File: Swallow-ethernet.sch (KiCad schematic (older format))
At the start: 35 parts, among them P1 XTAG2, P10 CONN_14, P11 CONN_8, P12 CONN_3, P13 GPIO_2, P14 GPIO_1, P2 XMP16_TR_Link, P3 TR_Link_Out, P4 Mode_Select, U1 25MHz_ASE_CLK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

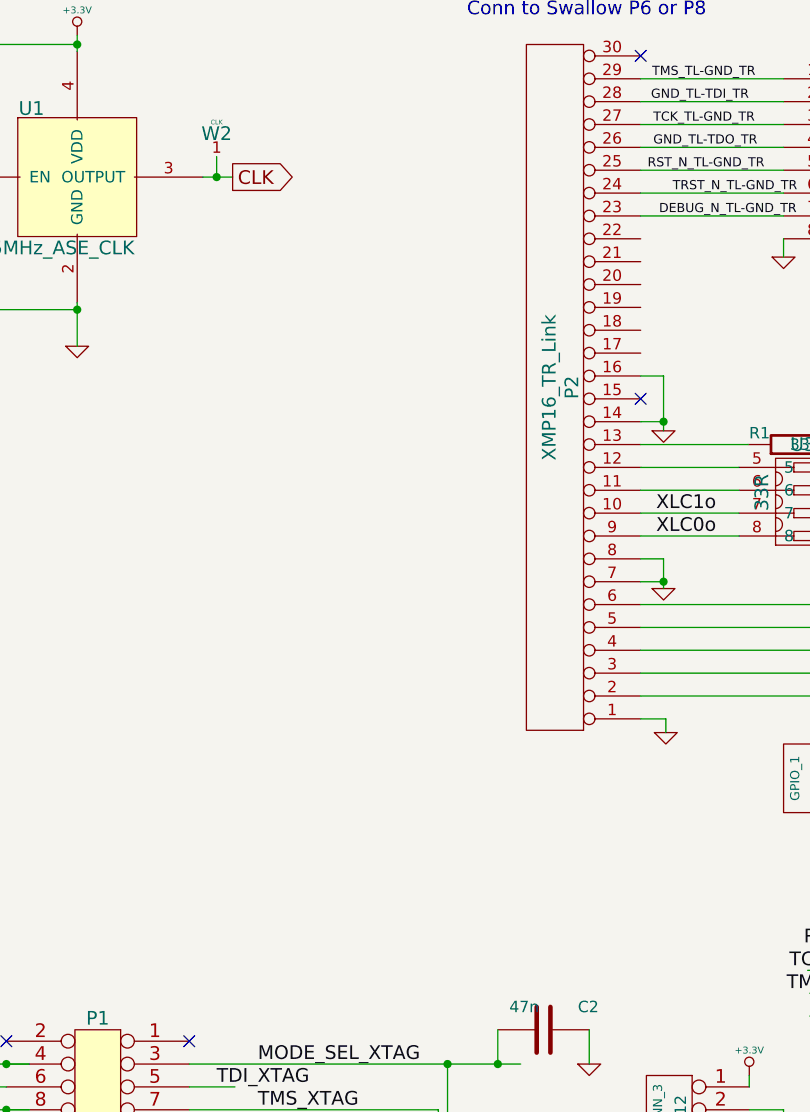
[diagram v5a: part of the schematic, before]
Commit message: Added clock buffer for L1 + ethernet MAC. Updated BOM.
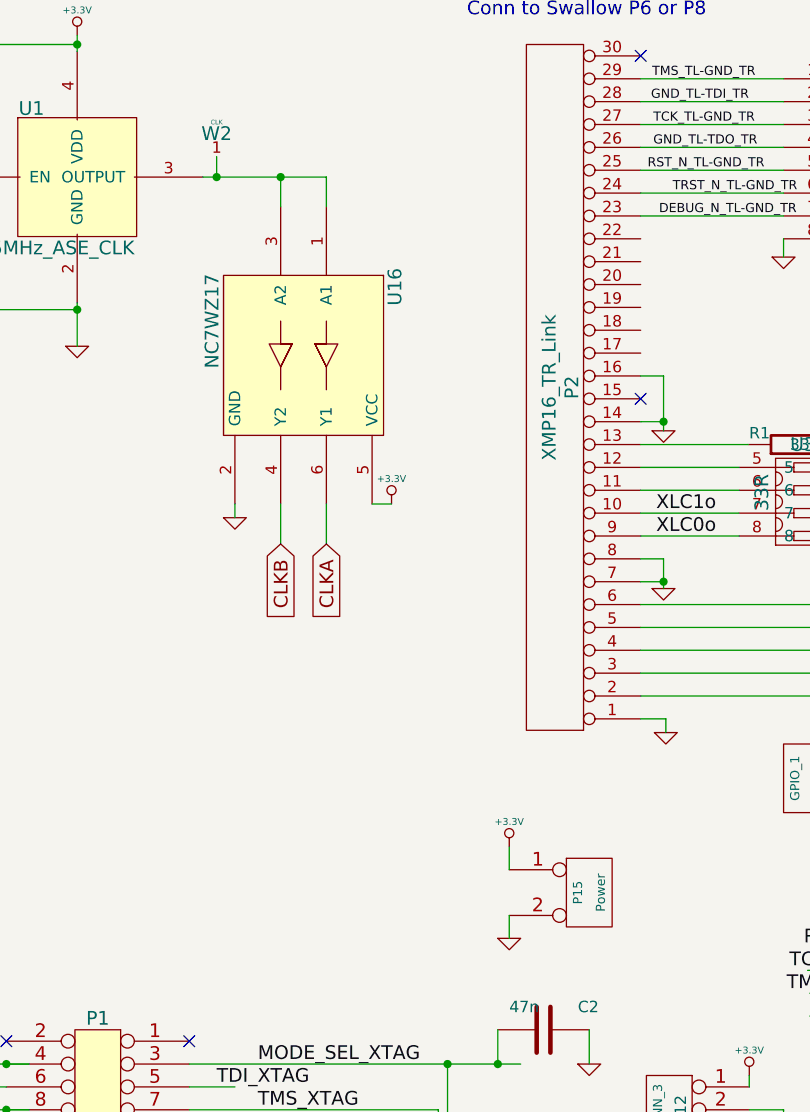
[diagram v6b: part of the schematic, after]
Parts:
- added P15: Power, symbol CONN_2
- added U16: NC7WZ17, symbol NC7WZ17
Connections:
- net labels added: CLKA, CLKB
- net labels removed: CLK
- wire segments 213 -> 221
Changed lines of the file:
@@
-EESchema Schematic File Version 2  date Thu 11 Oct 2012 12:37:16 BST
+EESchema Schematic File Version 2  date Thu 11 Oct 2012 17:02:03 BST
 LIBS:power
 LIBS:device
@@
 Comment4 ""
 $EndDescr
+Text GLabel 2750 2925 3    60   Input ~ 0
+CLKA
+Text GLabel 2550 2925 3    60   Input ~ 0
+CLKB
+Wire Wire Line
+	2750 2750 2750 2925
+Wire Wire Line
+	3035 2750 2950 2750
+Connection ~ 2550 1320
+Wire Wire Line
+	2210 1320 2750 1320
+Wire Wire Line
+	2750 1320 2750 1450
+Wire Wire Line
+	3550 4550 3550 4650
 Connection ~ 1250 740
 Connection ~ 1110 1260
@@
 Wire Wire Line
 	5115 2690 5285 2690
-Wire Wire Line
-	2210 1320 2340 1320
 Wire Wire Line
 	840  1030 840  740
@@
 Wire Notes Line
 	3450 7150 1450 7150
+Wire Wire Line
+	3550 4250 3550 4350
+Wire Wire Line
+	2550 1320 2550 1450
+Wire Wire Line
+	2350 2810 2350 2750
+Wire Wire Line
+	2550 2750 2550 2925
+$Comp
+L +3.3V #PWR5
+U 1 1 5076ECC9
+P 3035 2750
+F 0 "#PWR5" H 3035 2710 30  0001 C CNN
+F 1 "+3.3V" H 3035 2860 30  0000 C CNN
+	1    3035 2750
+	1    0    0    -1
+$EndComp
+$Comp
+L GND #PWR4
+U 1 1 5076ECC1
+P 2350 2810
+F 0 "#PWR4" H 2350 2810 30  0001 C CNN
+F 1 "GND" H 2350 2740 30  0001 C CNN
+	1    2350 2810
+	1    0    0    -1
+$EndComp
+$Comp
+L NC7WZ17 U16
+U 1 1 5076EC96
+P 2650 2100
+F 0 "U16" H 2350 2500 60  0000 C CNN
+F 1 "NC7WZ17" H 2500 1700 60  0000 C CNN
+	1    2650 2100
+	0    1    1    0
+$EndComp
+$Comp
+L +3.3V #PWR6
+U 1 1 5076E8F8
+P 3550 4250
+F 0 "#PWR6" H 3550 4210 30  0001 C CNN
+F 1 "+3.3V" H 3550 4360 30  0000 C CNN
+	1    3550 4250
+	1    0    0    -1
+$EndComp
+$Comp
+L GND #PWR7
+U 1 1 5076E8F3
+P 3550 4650
+F 0 "#PWR7" H 3550 4650 30  0001 C CNN
+F 1 "GND" H 3550 4580 30  0001 C CNN
+	1    3550 4650
+	1    0    0    -1
+$EndComp
+$Comp
+L CONN_2 P15
+U 1 1 5076E8EA
+P 3900 4450
+F 0 "P15" V 3850 4450 40  0000 C CNN
+F 1 "Power" V 3950 4450 40  0000 C CNN
+	1    3900 4450
+	1    0    0    -1
+$EndComp
 Text Notes 1750 7250 0    60   ~ 0
 Mechanicals
@@
 TMS_TL-GND_TR
 $Comp
-L +3.3V #PWR01
+L +3.3V #PWR13
 U 1 1 506DF2C0
 P 4600 5250
-F 0 "#PWR01" H 4600 5210 30  0001 C CNN
+F 0 "#PWR13" H 4600 5210 30  0001 C CNN
 F 1 "+3.3V" H 4600 5360 30  0000 C CNN
 	1    4600 5250
@@
 $EndComp
 $Comp
-L GND #PWR02
+L GND #PWR14
 U 1 1 506DF2B1
 P 4600 5550
-F 0 "#PWR02" H 4600 5550 30  0001 C CNN
+F 0 "#PWR14" H 4600 5550 30  0001 C CNN
 F 1 "GND" H 4600 5480 30  0001 C CNN
 	1    4600 5550
@@
 $EndComp
 $Comp
-L GND #PWR03
+L GND #PWR18
 U 1 1 506DF27B
 P 5850 5700
-F 0 "#PWR03" H 5850 5700 30  0001 C CNN
+F 0 "#PWR18" H 5850 5700 30  0001 C CNN
 F 1 "GND" H 5850 5630 30  0001 C CNN
 	1    5850 5700
@@
 $EndComp
 $Comp
-L +3.3V #PWR04
+L +3.3V #PWR17
 U 1 1 506DF26E
 P 5750 5550
-F 0 "#PWR04" H 5750 5510 30  0001 C CNN
+F 0 "#PWR17" H 5750 5510 30  0001 C CNN
 F 1 "+3.3V" H 5750 5660 30  0000 C CNN
 	1    5750 5550
@@
 $EndComp
 $Comp
-L GND #PWR05
+L GND #PWR16
 U 1 1 506DF266
 P 4750 6350
-F 0 "#PWR05" H 4750 6350 30  0001 C CNN
+F 0 "#PWR16" H 4750 6350 30  0001 C CNN
 F 1 "GND" H 4750 6280 30  0001 C CNN
 	1    4750 6350
@@
 $EndComp
 $Comp
-L GND #PWR06
+L GND #PWR15
 U 1 1 506D64CB
 P 4750 1670
-F 0 "#PWR06" H 4750 1670 30  0001 C CNN
+F 0 "#PWR15" H 4750 1670 30  0001 C CNN
 F 1 "GND" H 4750 1600 30  0001 C CNN
 	1    4750 1670
@@
 NoConn ~ 9815 910
 $Comp
-L GND #PWR07
+L GND #PWR24
 U 1 1 4F5BDE19
 P 9745 2550
-F 0 "#PWR07" H 9745 2550 30  0001 C CNN
+F 0 "#PWR24" H 9745 2550 30  0001 C CNN
 F 1 "GND" H 9745 2480 30  0001 C CNN
 	1    9745 2550
@@
 $EndComp
 $Comp
-L GND #PWR08
+L GND #PWR25
 U 1 1 506C85F4
 P 9815 3905
-F 0 "#PWR08" H 9815 3905 30  0001 C CNN
+F 0 "#PWR25" H 9815 3905 30  0001 C CNN
 F 1 "GND" H 9815 3835 30  0001 C CNN
 	1    9815 3905
@@
 $EndComp
 $Comp
-L +3.3V #PWR09
+L +3.3V #PWR19
 U 1 1 506A064F
 P 7185 4600
-F 0 "#PWR09" H 7185 4560 30  0001 C CNN
+F 0 "#PWR19" H 7185 4560 30  0001 C CNN
 F 1 "+3.3V" H 7185 4710 30  0000 C CNN
 	1    7185 4600
@@
 RESET_N
 $Comp
-L +3.3V #PWR010
+L +3.3V #PWR21
 U 1 1 506A0632
 P 8410 4970
-F 0 "#PWR010" H 8410 4930 30  0001 C CNN
+F 0 "#PWR21" H 8410 4930 30  0001 C CNN
 F 1 "+3.3V" H 8410 5080 30  0000 C CNN
 	1    8410 4970
@@
 $EndComp
 $Comp
-L GND #PWR011
+L GND #PWR20
 U 1 1 4F5BDEF3
 P 8355 4740
-F 0 "#PWR011" H 8355 4740 30  0001 C CNN
+F 0 "#PWR20" H 8355 4740 30  0001 C CNN
 F 1 "GND" H 8355 4670 30  0001 C CNN
 	1    8355 4740
@@
 $EndComp
 $Comp
-L GND #PWR012
+L GND #PWR23
 U 1 1 4F5BDE2C
 P 9715 3240
-F 0 "#PWR012" H 9715 3240 30  0001 C CNN
+F 0 "#PWR23" H 9715 3240 30  0001 C CNN
 F 1 "GND" H 9715 3170 30  0001 C CNN
 	1    9715 3240
@@
 $EndComp
 $Comp
-L GND #PWR013
+L GND #PWR30
 U 1 1 4F5BD965
 P 10490 5260
-F 0 "#PWR013" H 10490 5260 30  0001 C CNN
+F 0 "#PWR30" H 10490 5260 30  0001 C CNN
 F 1 "GND" H 10490 5190 30  0001 C CNN
 	1    10490 5260
@@
 $EndComp
 $Comp
-L GND #PWR014
+L GND #PWR27
 U 1 1 4F5BD8A9
 P 10050 6020
-F 0 "#PWR014" H 10050 6020 30  0001 C CNN
+F 0 "#PWR27" H 10050 6020 30  0001 C CNN
 F 1 "GND" H 10050 5950 30  0001 C CNN
 	1    10050 6020
@@
 $EndComp
 $Comp
-L GND #PWR015
+L GND #PWR29
 U 1 1 4F5BD89D
 P 10050 6980
-F 0 "#PWR015" H 10050 6980 30  0001 C CNN
+F 0 "#PWR29" H 10050 6980 30  0001 C CNN
 F 1 "GND" H 10050 6910 30  0001 C CNN
 	1    10050 6980
@@
 $EndComp
 $Comp
-L +3.3V #PWR016
+L +3.3V #PWR26
 U 1 1 4F5BD888
 P 10050 5260
-F 0 "#PWR016" H 10050 5220 30  0001 C CNN
+F 0 "#PWR26" H 10050 5220 30  0001 C CNN
 F 1 "+3.3V" H 10050 5370 30  0000 C CNN
 	1    10050 5260
@@
 RST_N_TL-GND_TR
 $Comp
-L GND #PWR017
+L GND #PWR12
 U 1 1 4F5BA318
 P 4235 3750
-F 0 "#PWR017" H 4235 3750 30  0001 C CNN
+F 0 "#PWR12" H 4235 3750 30  0001 C CNN
 F 1 "GND" H 4235 3680 30  0001 C CNN
 	1    4235 3750
@@
 $EndComp
 $Comp
-L GND #PWR018
+L GND #PWR10
 U 1 1 4F5BA2F7
 P 4225 2430
-F 0 "#PWR018" H 4225 2430 30  0001 C CNN
+F 0 "#PWR10" H 4225 2430 30  0001 C CNN
 F 1 "GND" H 4225 2360 30  0001 C CNN
 	1    4225 2430
@@
 $EndComp
 $Comp
-L GND #PWR019
+L GND #PWR11
 U 1 1 4F5BA2E3
 P 4225 3120
-F 0 "#PWR019" H 4225 3120 30  0001 C CNN
+F 0 "#PWR11" H 4225 3120 30  0001 C CNN
 F 1 "GND" H 4225 3050 30  0001 C CNN
 	1    4225 3120
@@
 $EndComp
 $Comp
-L GND #PWR020
+L GND #PWR3
 U 1 1 4F5B92B3
 P 1660 2060
-F 0 "#PWR020" H 1660 2060 30  0001 C CNN
+F 0 "#PWR3" H 1660 2060 30  0001 C CNN
 F 1 "GND" H 1660 1990 30  0001 C CNN
 	1    1660 2060
 	1    0    0    -1
 $EndComp
-Text GLabel 2340 1320 2    60   Output ~ 0
-CLK
-$Comp
-L +3.3V #PWR021
+$Comp
+L +3.3V #PWR2
 U 1 1 4F57E8BD
 P 1660 700
-F 0 "#PWR021" H 1660 660 30  0001 C CNN
+F 0 "#PWR2" H 1660 660 30  0001 C CNN
 F 1 "+3.3V" H 1660 810 30  0000 C CNN
 	1    1660 700
@@
 XL1o_XTAG
 $Comp
-L +3.3V #PWR022
+L +3.3V #PWR28
 U 1 1 4EDA7F39
 P 10050 6250
-F 0 "#PWR022" H 10050 6210 30  0001 C CNN
+F 0 "#PWR28" H 10050 6210 30  0001 C CNN
 F 1 "+3.3V" H 10050 6360 30  0000 C CNN
 	1    10050 6250
@@
 NoConn ~ 1350 5100
 $Comp
-L GND #PWR023
+L GND #PWR9
 U 1 1 4ED12818
 P 3900 5200
-F 0 "#PWR023" H 3900 5200 30  0001 C CNN
+F 0 "#PWR9" H 3900 5200 30  0001 C CNN
 F 1 "GND" H 3900 5130 30  0001 C CNN
 	1    3900 5200
@@
 $EndComp
 $Comp
-L GND #PWR024
+L GND #PWR22
 U 1 1 4ED12726
 P 8550 7050
-F 0 "#PWR024" H 8550 7050 30  0001 C CNN
+F 0 "#PWR22" H 8550 7050 30  0001 C CNN
 F 1 "GND" H 8550 6980 30  0001 C CNN
 	1    8550 7050
@@
 MODE_SEL_XTAG
 $Comp
-L +3.3V #PWR025
+L +3.3V #PWR8
 U 1 1 4ED0380D
 P 3840 5540
-F 0 "#PWR025" H 3840 5500 30  0001 C CNN
+F 0 "#PWR8" H 3840 5500 30  0001 C CNN
 F 1 "+3.3V" H 3840 5650 30  0000 C CNN
 	1    3840 5540
@@
 $EndComp
 $Comp
-L GND #PWR026
+L GND #PWR1
 U 1 1 4ED034D6
 P 1250 6250
-F 0 "#PWR026" H 1250 6250 30  0001 C CNN
+F 0 "#PWR1" H 1250 6250 30  0001 C CNN
 F 1 "GND" H 1250 6180 30  0001 C CNN
 	1    1250 6250

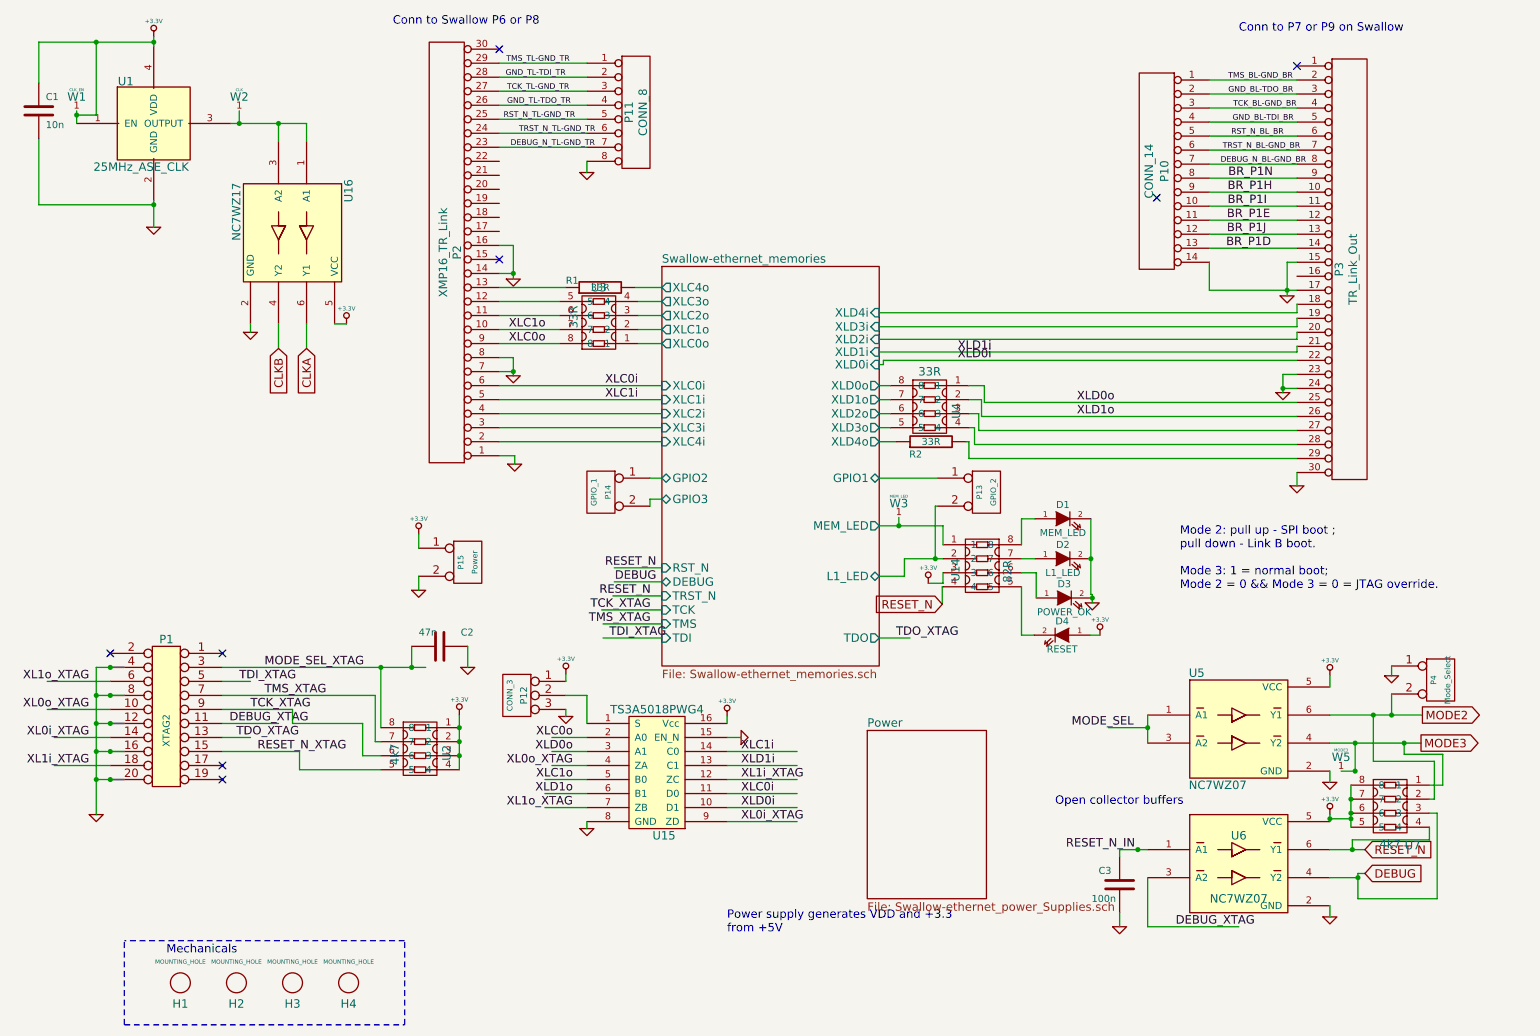
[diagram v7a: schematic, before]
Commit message: V2 begin. Bugs fixed and pushed to layout * RESET_N_IN => RESET_N_XTAG and associated wire connection * Fixed silkscreen P10 Pin 1 "GND" => "TMS" * Fixed unconnected ground link vias above P5
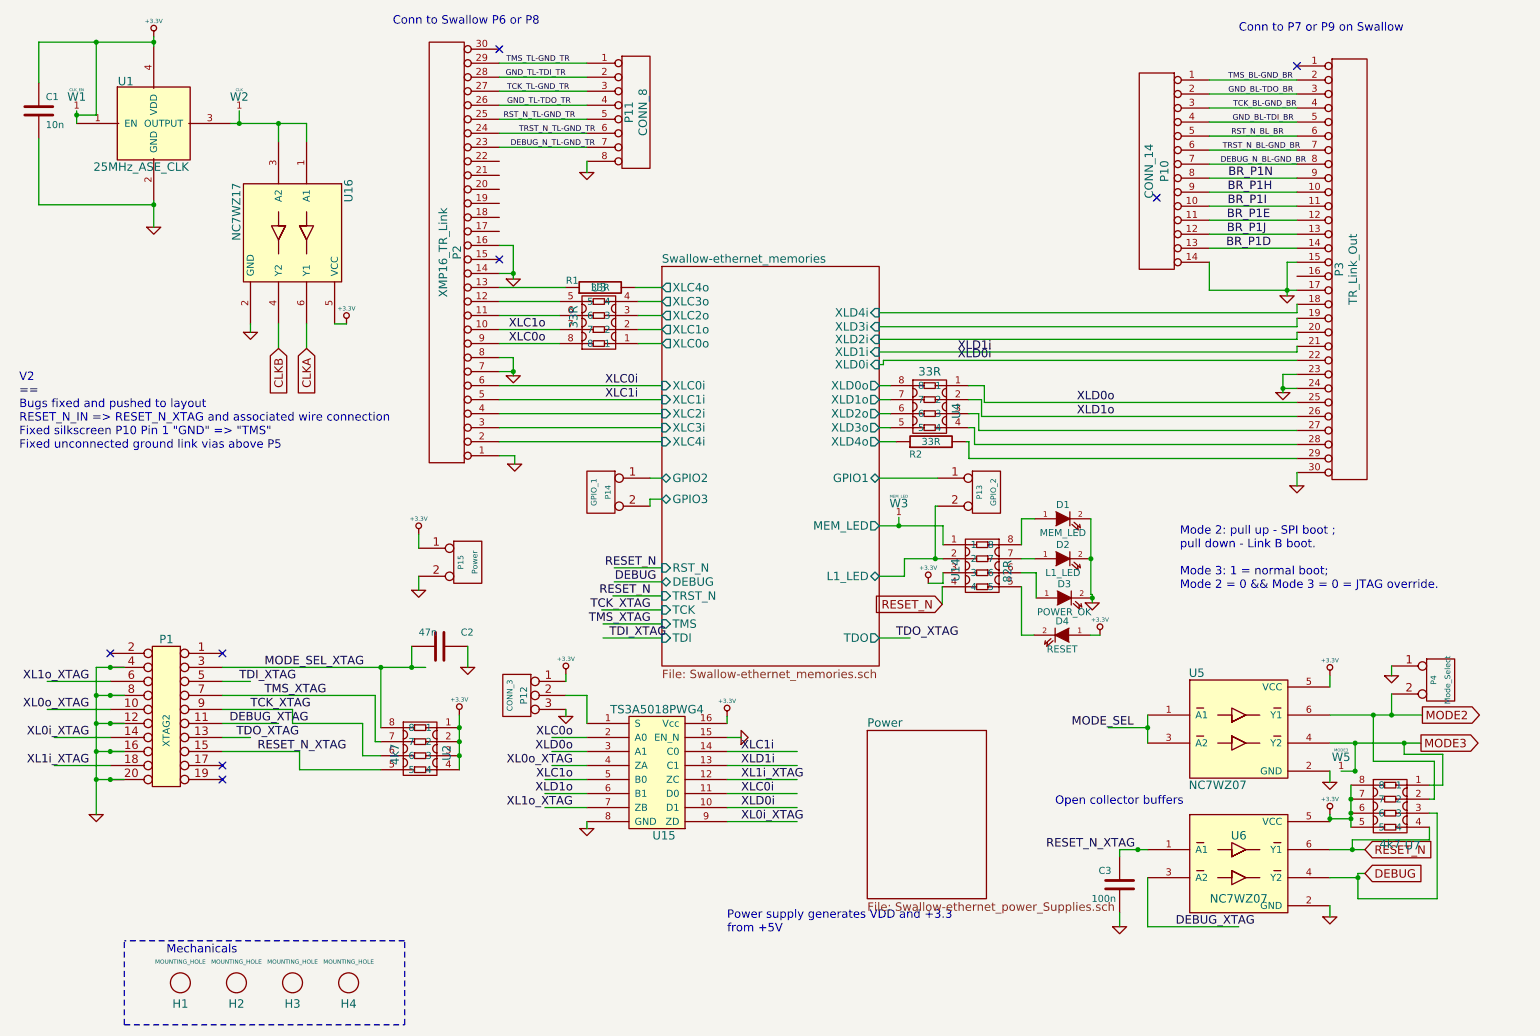
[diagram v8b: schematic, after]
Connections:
- net labels removed: RESET_N_IN
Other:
- note added: "V2\n==\nBugs fixed and pushed to layout\nRESET_N_IN => RESET_N_XTAG and associated wire connection\nFixed silkscreen P10 Pin 1 "GND" => "TMS"\nFixed unconnected ground link vias above P5"
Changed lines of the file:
@@
-EESchema Schematic File Version 2  date Tue 16 Oct 2012 12:12:08 BST
+EESchema Schematic File Version 2  date Mon 19 Nov 2012 21:12:34 GMT
 LIBS:power
 LIBS:device
@@
 LIBS:testpoints
 LIBS:Swallow-ethernet-cache
-EELAYER 25  0
+EELAYER 27 0
 EELAYER END
-$Descr A4 11700 8267
+$Descr A4 11693 8268
 encoding utf-8
 Sheet 1 4
 Title "noname.sch"
-Date "16 oct 2012"
+Date "19 nov 2012"
 Rev ""
 Comp ""
@@
 $EndComp
 Text Label 8660 6500 2    60   ~ 0
-RESET_N_IN
+RESET_N_XTAG
 Text Label 4455 2790 2    60   ~ 0
 XLC1o
@@
 	1    0    0    -1
 $EndComp
+Text Notes 700  3650 0    60   ~ 0
+V2\n==\nBugs fixed and pushed to layout\nRESET_N_IN => RESET_N_XTAG and associated wire connection\nFixed silkscreen P10 Pin 1 "GND" => "TMS"\nFixed unconnected ground link vias above P5
 $EndSCHEMATC
